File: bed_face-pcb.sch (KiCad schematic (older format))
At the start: 112 parts, among them J1 BATTERY, SW1 RESET, U1 ProMicro

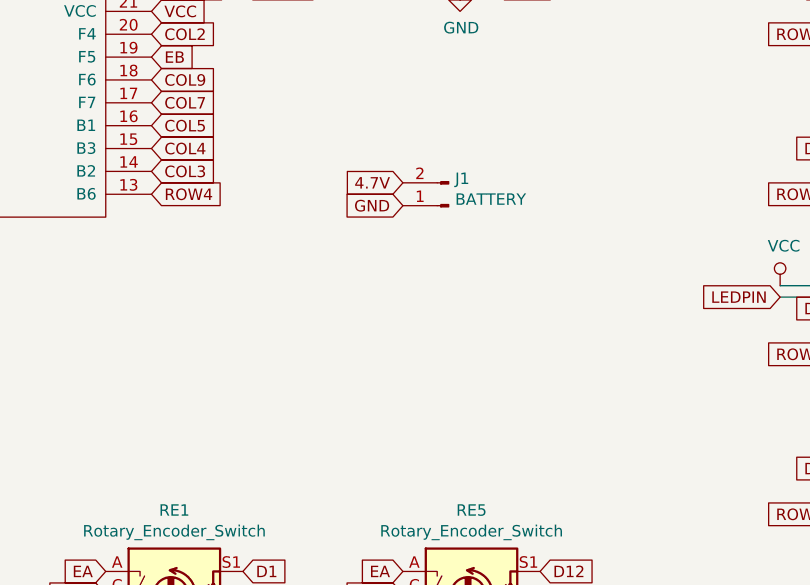
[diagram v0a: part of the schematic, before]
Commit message: added pads to f.mask, changed footprint silks, make SW1 th
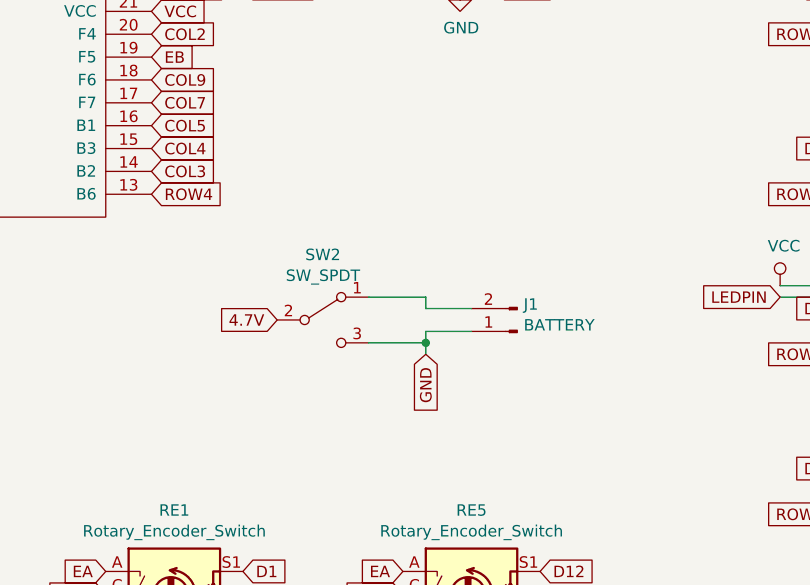
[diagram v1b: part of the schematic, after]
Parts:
- added SW2: SW_SPDT, symbol Switch:SW_SPDT
- D1, D10, D11, D12, D13, D14, D15, D16, D17, D18, D19, D2, D20, D21, D22, D23, D24, D25, D26, D27, D28, D29, D3, D30, D31, D32, D33, D34, D35, D36, D37, D38, D39, D4, D40, D41, D42, D43, D44, D45, D46, D47, D48, D5, D6, D7, D8, D9: footprint Keebio-Parts:Diode-Hybrid-Back -> bed-face-components:Diode-Hybrid-Back-EDIT
- RE1, RE2, RE3, RE4, RE5, RE6, RE7, RE8: footprint reversible-kicad-footprints:MX-1U-EC11_Switch -> bed-face-components:EC11_Switch-EDIT
- SW1: footprint Keebio-Parts:SW_SPST_TL3342 -> random-keyboard-parts:PushButton_6x6mm_TH
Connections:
- net 4.7V: now also SW2.2 (B); no longer J1.2 (Pin_2)
- net GND: now also SW2.3 (C)
- new net: J1.2 (Pin_2), SW2.1 (A)
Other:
- moved on the sheet: J1

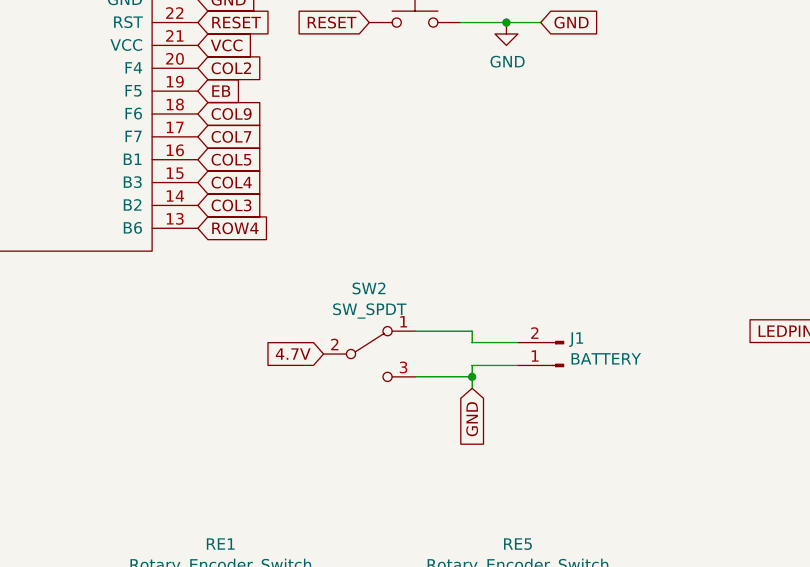
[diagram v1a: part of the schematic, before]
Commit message: added miniature power switch * TODO closely check power pinout
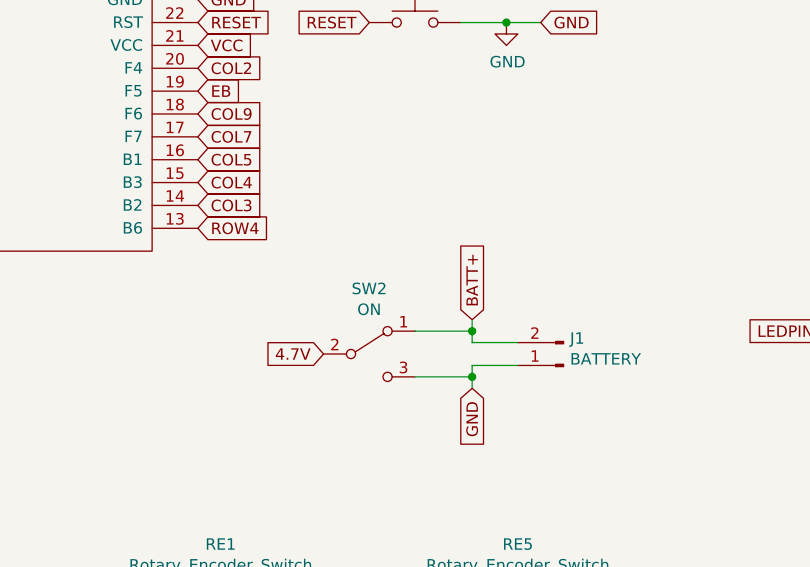
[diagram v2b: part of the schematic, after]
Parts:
- SW1: footprint random-keyboard-parts:PushButton_6x6mm_TH -> random-keyboard-parts:SKQG-1155865
- SW2: value SW_SPDT -> ON; footprint (none) -> bed-face-components:SWITCH_SPST_SMD_A-EDIT
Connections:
- net BATT+: now reaches J1.2 (Pin_2), SW2.1 (A)
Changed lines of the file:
@@
 F 0 "SW1" H 4250 1985 50  0000 C CNN
 F 1 "RESET" H 4250 1894 50  0000 C CNN
-F 2 "random-keyboard-parts:PushButton_6x6mm_TH" H 4250 1900 50  0001 C CNN
+F 2 "random-keyboard-parts:SKQG-1155865" H 4250 1900 50  0001 C CNN
 F 3 "~" H 4250 1900 50  0001 C CNN
 	1    4250 1700
@@
 P 4050 3150
 F 0 "SW2" H 4050 3435 50  0000 C CNN
-F 1 "SW_SPDT" H 4050 3344 50  0000 C CNN
-F 2 "" H 4050 3150 50  0001 C CNN
+F 1 "ON" H 4050 3344 50  0000 C CNN
+F 2 "bed-face-components:SWITCH_SPST_SMD_A-EDIT" H 4050 3150 50  0001 C CNN
 F 3 "~" H 4050 3150 50  0001 C CNN
 	1    4050 3150
@@
 	4500 3250 4500 3300
 Connection ~ 4500 3250
+Text GLabel 4500 3000 1    50   Input ~ 0
+BATT+
+Wire Wire Line
+	4500 3000 4500 3050
+Connection ~ 4500 3050
 $EndSCHEMATC

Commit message: finished tracking
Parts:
- MX41: footprint bed-face-components:MXOnly-1U-NoLED-EDIT -> bed-face-components:MXOnly-1U-2U-EDIT-LOWER
- MX44: footprint bed-face-components:MXOnly-1U-NoLED-EDIT -> bed-face-components:MXOnly-1U-2U-EDIT-RAISE
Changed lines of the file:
@@
 F 0 "MX44" H 9883 3873 60  0000 C CNN
 F 1 "RAISE" H 9883 3799 20  0000 C CNN
-F 2 "bed-face-components:MXOnly-1U-NoLED-EDIT" H 9225 3625 60  0001 C CNN
+F 2 "bed-face-components:MXOnly-1U-2U-EDIT-RAISE" H 9225 3625 60  0001 C CNN
 F 3 "" H 9225 3625 60  0001 C CNN
 	1    9850 3650
@@
 F 0 "MX41" H 8533 3873 60  0000 C CNN
 F 1 "LOWER" H 8533 3799 20  0000 C CNN
-F 2 "bed-face-components:MXOnly-1U-NoLED-EDIT" H 7875 3625 60  0001 C CNN
+F 2 "bed-face-components:MXOnly-1U-2U-EDIT-LOWER" H 7875 3625 60  0001 C CNN
 F 3 "" H 7875 3625 60  0001 C CNN
 	1    8500 3650
